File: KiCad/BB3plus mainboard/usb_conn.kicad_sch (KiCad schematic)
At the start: 55 parts, among them IC18 MIC2026A-1YM-TR, IC19 PTN5150AHXMP, IC20 TPS2068E, IC21 TPD2E001DRLR, IC22 TPD2E001DRLR, IC23 FUSB340TMX, Q7 2N7002, Q8 2N7002, X14 USB4056-03-A, X15 MGB0A1-1CDDB005H

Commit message: PE fault detection section updated
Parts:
- renumbered C111 to C112, C112 to C113, C113 to C114, C114 to C115, C115 to C116, C116 to C117, C117 to C118, C118 to C119, C119 to C120, C120 to C121, C121 to C122, C122 to C123, C123 to C124, C124 to C125, C125 to C126, C126 to C127, JP14 to JP16, JP15 to JP17, JP16 to JP18, JP17 to JP19
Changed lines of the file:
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@@
 		(in_pos_files yes)
 		(dnp no)
-		(property "Reference" "C116"
+		(property "Reference" "C117"
 			(at 94.234 84.074 0)
 			(show_name no)
@@
 			(project "BB3plus mainboard"
 				(path "/1df84e4f-233a-4f72-9418-c0020706bb76/c0a485a3-023d-4313-ae06-c16e1fdbf75a"
-					(reference "C116")
+					(reference "C117")
 					(unit 1)
 				)
@@
 		(in_pos_files yes)
 		(dnp no)
-		(property "Reference" "C115"
+		(property "Reference" "C116"
 			(at 85.725 142.875 0)
 			(show_name no)
@@
 			(project "BB3plus mainboard"
 				(path "/1df84e4f-233a-4f72-9418-c0020706bb76/c0a485a3-023d-4313-ae06-c16e1fdbf75a"
-					(reference "C115")
+					(reference "C116")
 					(unit 1)
 				)
@@
 		(in_pos_files yes)
 		(dnp no)
-		(property "Reference" "C117"
+		(property "Reference" "C118"
 			(at 109.474 68.834 0)
 			(show_name no)
@@
 			(project "BB3plus mainboard"
 				(path "/1df84e4f-233a-4f72-9418-c0020706bb76/c0a485a3-023d-4313-ae06-c16e1fdbf75a"
-					(reference "C117")
+					(reference "C118")
 					(unit 1)
 				)
@@
 		(in_pos_files yes)
 		(dnp no)
-		(property "Reference" "C125"
+		(property "Reference" "C126"
 			(at 228.6 60.325 90)
 			(show_name no)
@@
 			(project "BB3plus mainboard"
 				(path "/1df84e4f-233a-4f72-9418-c0020706bb76/c0a485a3-023d-4313-ae06-c16e1fdbf75a"
-					(reference "C125")
+					(reference "C126")
 					(unit 1)
 				)
@@
 		(in_pos_files yes)
 		(dnp no)
-		(property "Reference" "C122"
+		(property "Reference" "C123"
 			(at 228.6 42.545 90)
 			(show_name no)
@@
 			(project "BB3plus mainboard"
 				(path "/1df84e4f-233a-4f72-9418-c0020706bb76/c0a485a3-023d-4313-ae06-c16e1fdbf75a"
-					(reference "C122")
+					(reference "C123")
 					(unit 1)
 				)
@@
 		(in_pos_files yes)
 		(dnp no)
-		(property "Reference" "JP14"
+		(property "Reference" "JP16"
 			(at 59.69 67.31 0)
 			(show_name no)
@@
 			(project "BB3plus mainboard"
 				(path "/1df84e4f-233a-4f72-9418-c0020706bb76/c0a485a3-023d-4313-ae06-c16e1fdbf75a"
-					(reference "JP14")
+					(reference "JP16")
 					(unit 1)
 				)
@@
 		(in_pos_files yes)
 		(dnp no)
-		(property "Reference" "#SUPPLY065"
+		(property "Reference" "#SUPPLY068"
 			(at 177.8 73.66 0)
 			(hide yes)
@@
 			(project "BB3plus mainboard"
 				(path "/1df84e4f-233a-4f72-9418-c0020706bb76/c0a485a3-023d-4313-ae06-c16e1fdbf75a"
-					(reference "#SUPPLY065")
+					(reference "#SUPPLY068")
 					(unit 1)
 				)
@@
 		(in_pos_files yes)
 		(dnp no)
-		(property "Reference" "C111"
+		(property "Reference" "C112"
 			(at 28.575 34.29 0)
 			(show_name no)
@@
 			(project "BB3plus mainboard"
 				(path "/1df84e4f-233a-4f72-9418-c0020706bb76/c0a485a3-023d-4313-ae06-c16e1fdbf75a"
-					(reference "C111")
+					(reference "C112")
 					(unit 1)
 				)
@@
 		(in_pos_files yes)
 		(dnp no)
-		(property "Reference" "#SUPPLY067"
+		(property "Reference" "#SUPPLY070"
 			(at 205.74 73.66 0)
 			(hide yes)
@@
 			(project "BB3plus mainboard"
 				(path "/1df84e4f-233a-4f72-9418-c0020706bb76/c0a485a3-023d-4313-ae06-c16e1fdbf75a"
-					(reference "#SUPPLY067")
+					(reference "#SUPPLY070")
 					(unit 1)
 				)
@@
 		(in_pos_files yes)
 		(dnp no)
-		(property "Reference" "C112"
+		(property "Reference" "C113"
 			(at 35.56 31.75 0)
 			(show_name no)
@@
 			(project "BB3plus mainboard"
 				(path "/1df84e4f-233a-4f72-9418-c0020706bb76/c0a485a3-023d-4313-ae06-c16e1fdbf75a"
-					(reference "C112")
+					(reference "C113")
 					(unit 1)
 				)
@@
 		(in_pos_files yes)
 		(dnp no)
-		(property "Reference" "JP17"
+		(property "Reference" "JP19"
 			(at 59.69 90.17 0)
 			(show_name no)
@@
 			(project "BB3plus mainboard"
 				(path "/1df84e4f-233a-4f72-9418-c0020706bb76/c0a485a3-023d-4313-ae06-c16e1fdbf75a"
-					(reference "JP17")
+					(reference "JP19")
 					(unit 1)
 				)
@@
 		(in_pos_files yes)
 		(dnp no)
-		(property "Reference" "JP15"
+		(property "Reference" "JP17"
 			(at 59.69 72.39 0)
 			(show_name no)
@@
 			(project "BB3plus mainboard"
 				(path "/1df84e4f-233a-4f72-9418-c0020706bb76/c0a485a3-023d-4313-ae06-c16e1fdbf75a"
-					(reference "JP15")
+					(reference "JP17")
 					(unit 1)
 				)
@@
 		(in_pos_files yes)
 		(dnp no)
-		(property "Reference" "C121"
+		(property "Reference" "C122"
 			(at 155.194 45.974 0)
 			(show_name no)
@@
 			(project "BB3plus mainboard"
 				(path "/1df84e4f-233a-4f72-9418-c0020706bb76/c0a485a3-023d-4313-ae06-c16e1fdbf75a"
-					(reference "C121")
+					(reference "C122")
 					(unit 1)
 				)
@@
 		(in_pos_files yes)
 		(dnp no)
-		(property "Reference" "#SUPPLY064"
+		(property "Reference" "#SUPPLY067"
 			(at 177.8 43.18 0)
 			(hide yes)
@@
 			(project "BB3plus mainboard"
 				(path "/1df84e4f-233a-4f72-9418-c0020706bb76/c0a485a3-023d-4313-ae06-c16e1fdbf75a"
-					(reference "#SUPPLY064")
+					(reference "#SUPPLY067")
 					(unit 1)
 				)
@@
 		(in_pos_files yes)
 		(dnp no)
-		(property "Reference" "C119"
+		(property "Reference" "C120"
 			(at 116.84 45.72 0)
 			(show_name no)
@@
 			(project "BB3plus mainboard"
 				(path "/1df84e4f-233a-4f72-9418-c0020706bb76/c0a485a3-023d-4313-ae06-c16e1fdbf75a"
-					(reference "C119")
+					(reference "C120")
 					(unit 1)
 				)
@@
 		(in_pos_files yes)
 		(dnp no)
-		(property "Reference" "C113"
+		(property "Reference" "C114"
 			(at 48.26 167.005 0)
 			(show_name no)
@@
 			(project "BB3plus mainboard"
 				(path "/1df84e4f-233a-4f72-9418-c0020706bb76/c0a485a3-023d-4313-ae06-c16e1fdbf75a"
-					(reference "C113")
+					(reference "C114")
 					(unit 1)
 				)
@@
 		(in_pos_files yes)
 		(dnp no)
-		(property "Reference" "JP16"
+		(property "Reference" "JP18"
 			(at 59.69 77.47 0)
 			(show_name no)
@@
 			(project "BB3plus mainboard"
 				(path "/1df84e4f-233a-4f72-9418-c0020706bb76/c0a485a3-023d-4313-ae06-c16e1fdbf75a"
-					(reference "JP16")
+					(reference "JP18")
 					(unit 1)
 				)
@@
 		(in_pos_files yes)
 		(dnp no)
-		(property "Reference" "C126"
+		(property "Reference" "C127"
 			(at 271.78 37.465 90)
 			(show_name no)
@@
 			(project "BB3plus mainboard"
 				(path "/1df84e4f-233a-4f72-9418-c0020706bb76/c0a485a3-023d-4313-ae06-c16e1fdbf75a"
-					(reference "C126")
+					(reference "C127")
 					(unit 1)
 				)
@@
 		(in_pos_files yes)
 		(dnp no)
-		(property "Reference" "C118"
+		(property "Reference" "C119"
 			(at 109.474 84.074 0)
 			(show_name no)
@@
 			(project "BB3plus mainboard"
 				(path "/1df84e4f-233a-4f72-9418-c0020706bb76/c0a485a3-023d-4313-ae06-c16e1fdbf75a"
-					(reference "C118")
+					(reference "C119")
 					(unit 1)
 				)
@@
 		(in_pos_files yes)
 		(dnp no)
-		(property "Reference" "#SUPPLY066"
+		(property "Reference" "#SUPPLY069"
 			(at 205.74 43.18 0)
 			(hide yes)
@@
 			(project "BB3plus mainboard"
 				(path "/1df84e4f-233a-4f72-9418-c0020706bb76/c0a485a3-023d-4313-ae06-c16e1fdbf75a"
-					(reference "#SUPPLY066")
+					(reference "#SUPPLY069")
 					(unit 1)
 				)
@@
 		(in_pos_files yes)
 		(dnp no)
-		(property "Reference" "C123"
+		(property "Reference" "C124"
 			(at 228.6 45.085 90)
 			(show_name no)
@@
 			(project "BB3plus mainboard"
 				(path "/1df84e4f-233a-4f72-9418-c0020706bb76/c0a485a3-023d-4313-ae06-c16e1fdbf75a"
-					(reference "C123")
+					(reference "C124")
 					(unit 1)
 				)
@@
 		(in_pos_files yes)
 		(dnp no)
-		(property "Reference" "C120"
+		(property "Reference" "C121"
 			(at 127 95.885 90)
 			(show_name no)
@@
 			(project "BB3plus mainboard"
 				(path "/1df84e4f-233a-4f72-9418-c0020706bb76/c0a485a3-023d-4313-ae06-c16e1fdbf75a"
-					(reference "C120")
+					(reference "C121")
 					(unit 1)
 				)
@@
 		(in_pos_files yes)
 		(dnp no)
-		(property "Reference" "C124"
+		(property "Reference" "C125"
 			(at 228.6 57.785 90)
 			(show_name no)
@@
 			(project "BB3plus mainboard"
 				(path "/1df84e4f-233a-4f72-9418-c0020706bb76/c0a485a3-023d-4313-ae06-c16e1fdbf75a"
-					(reference "C124")
+					(reference "C125")
 					(unit 1)
 				)
@@
 		(in_pos_files yes)
 		(dnp no)
-		(property "Reference" "C114"
+		(property "Reference" "C115"
 			(at 85.725 130.175 0)
 			(show_name no)
@@
 			(project "BB3plus mainboard"
 				(path "/1df84e4f-233a-4f72-9418-c0020706bb76/c0a485a3-023d-4313-ae06-c16e1fdbf75a"
-					(reference "C114")
+					(reference "C115")
 					(unit 1)
 				)

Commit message: Various small changes
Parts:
- R78: now fitted; now in the parts list
- renumbered JP18 to JP16, JP16 to JP17, JP17 to JP18, X14 to X15, X15 to X16
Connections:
- net USBC_CONN_DET: no longer R78.2
- net at IC19.5 (ADR/CON_DET), JP16.1: now also R78.2
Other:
- moved on the sheet: JP16, TP13

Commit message: #24
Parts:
- D8: renamed from D14; now not fitted; now left out of the parts list
- renumbered C112 to C110, C113 to C111, C114 to C112, C115 to C113, C116 to C114, C117 to C115, C118 to C116, C119 to C117, C120 to C118, C121 to C119, C122 to C120, C123 to C121, C124 to C122, C125 to C123, C126 to C124, C127 to C125, IC18 to IC15, IC19 to IC16, IC20 to IC17, IC21 to IC18, IC22 to IC19, IC23 to IC20, JP16 to JP15, JP17 to JP16, JP18 to JP17, JP19 to JP18, R78 to R75, R79 to R76, R80 to R77, R81 to R78, R82 to R79, R83 to R80, R84 to R81, R85 to R82, R86 to R83, R87 to R84, R88 to R85, R89 to R86, R90 to R87

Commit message: USB CC wiring updated
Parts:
- removed JP18: 10129378-902001BLF, PCM_EEZ_SMD:JP2 open (0603), symbol PCM_EEZ_unsorted:JP2 open
- added JP15: (no value), PCM_EEZ_SMD:JP3 shorted (0603), symbol PCM_EEZ_unsorted:JP3 shorted
- added R78: 10K, PCM_EEZ_passives:R_0603_1608Metric, symbol PCM_EEZ_passives:R-EU
- C110, C113, C114: LCSC - -> C336508
- JP16: renamed from JP15; value 10129378-902001BLF -> (none); DigiKey 10129378-902001BLF-ND -> (none); LCSC C3324910 -> (none); Label I2C HUB -> (none); Mouser 649-1012937890201BLF -> (none); TME ZL201-02G -> (none)
- JP17: renamed from JP16; value 10129378-902001BLF -> (none); footprint PCM_EEZ_SMD:JP2 open (0603) -> PCM_EEZ_SMD:JP2 shorted (0603); symbol PCM_EEZ_unsorted:JP2 open -> PCM_EEZ_unsorted:JP2 shorted; DigiKey 10129378-902001BLF-ND -> (none); LCSC C3324910 -> (none); Mouser 649-1012937890201BLF -> (none); TME ZL201-02G -> (none)
- JP18: renamed from JP17; value 10129378-902001BLF -> (none); footprint PCM_EEZ_SMD:JP2 open (0603) -> PCM_EEZ_SMD:JP2 shorted (0603); symbol PCM_EEZ_unsorted:JP2 open -> PCM_EEZ_unsorted:JP2 shorted; DigiKey 10129378-902001BLF-ND -> (none); LCSC C3324910 -> (none); Label I2C HUB -> (none); Mouser 649-1012937890201BLF -> (none); TME ZL201-02G -> (none)
- LED7: now fitted
- R85: renamed from R84; value 1K -> 1K8; DigiKey 13-RC0603FR-131KLCT-ND -> 13-RC0603FR-131K8LCT-ND; LCSC C21190 -> C4177; Mouser 603-RC0603FR-131KL -> 603-RC0603FR-131K8L; TME CQ0603-1K-1% -> SMD0603-1K8-1%; now fitted; now in the parts list
- X15: Label USB-C DRD -> USB-C
- renumbered R78 to R79, R79 to R80, R80 to R81, R81 to R82, R82 to R83, R83 to R84, R85 to R86, R86 to R87, R87 to R88
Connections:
- net +3V3: now also JP15.NO, R78.1; no longer R75.1
- net GND: now also JP15.NC
- net at IC16.3 (PORT): now also R78.2
- new net: JP15.COM, R75.1
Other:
- moved on the sheet: JP16, R75

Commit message: #25
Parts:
- X15: value USB4056-03-A -> USB4080-03-A; footprint PCM_EEZ_connectors:USB4056-03-A_REVA2 -> PCM_EEZ_connectors:USB4080-03-A_REVA1; DigiKey 2073-USB4056-03-ACT-ND -> 2073-USB4080-03-ACT-ND; LCSC C7407280 -> C48533151; Mouser 640-USB4056-03-A -> 640-USB4080-03-A; TME USB4056-03-A -> USB4080-03-A
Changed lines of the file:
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@@
 			)
 		)
-		(property "Value" "USB4056-03-A"
+		(property "Value" "USB4080-03-A"
 			(at 137.795 92.075 0)
 			(show_name no)
@@
 			)
 		)
-		(property "Footprint" "PCM_EEZ_connectors:USB4056-03-A_REVA2"
+		(property "Footprint" "PCM_EEZ_connectors:USB4080-03-A_REVA1"
 			(at 147.32 99.06 0)
 			(hide yes)
@@
 			)
 		)
-		(property "Description" "USB-C USB 3.2 Rec, Horz, Hybrid PCB Top Mount, T+R"
+		(property "Description" ""
 			(at 147.32 96.52 0)
 			(hide yes)
@@
 			)
 		)
-		(property "DigiKey" "2073-USB4056-03-ACT-ND"
+		(property "DigiKey" "2073-USB4080-03-ACT-ND"
 			(at 147.32 101.6 0)
 			(hide yes)
@@
 			)
 		)
-		(property "Mouser" "640-USB4056-03-A"
+		(property "Mouser" "640-USB4080-03-A"
 			(at 147.32 104.14 0)
 			(hide yes)
@@
 			)
 		)
-		(property "TME" "USB4056-03-A"
+		(property "TME" "USB4080-03-A"
 			(at 147.32 106.68 0)
 			(hide yes)
@@
 			)
 		)
-		(property "LCSC" "C7407280"
+		(property "LCSC" "C48533151"
 			(at 147.32 109.22 0)
 			(hide yes)

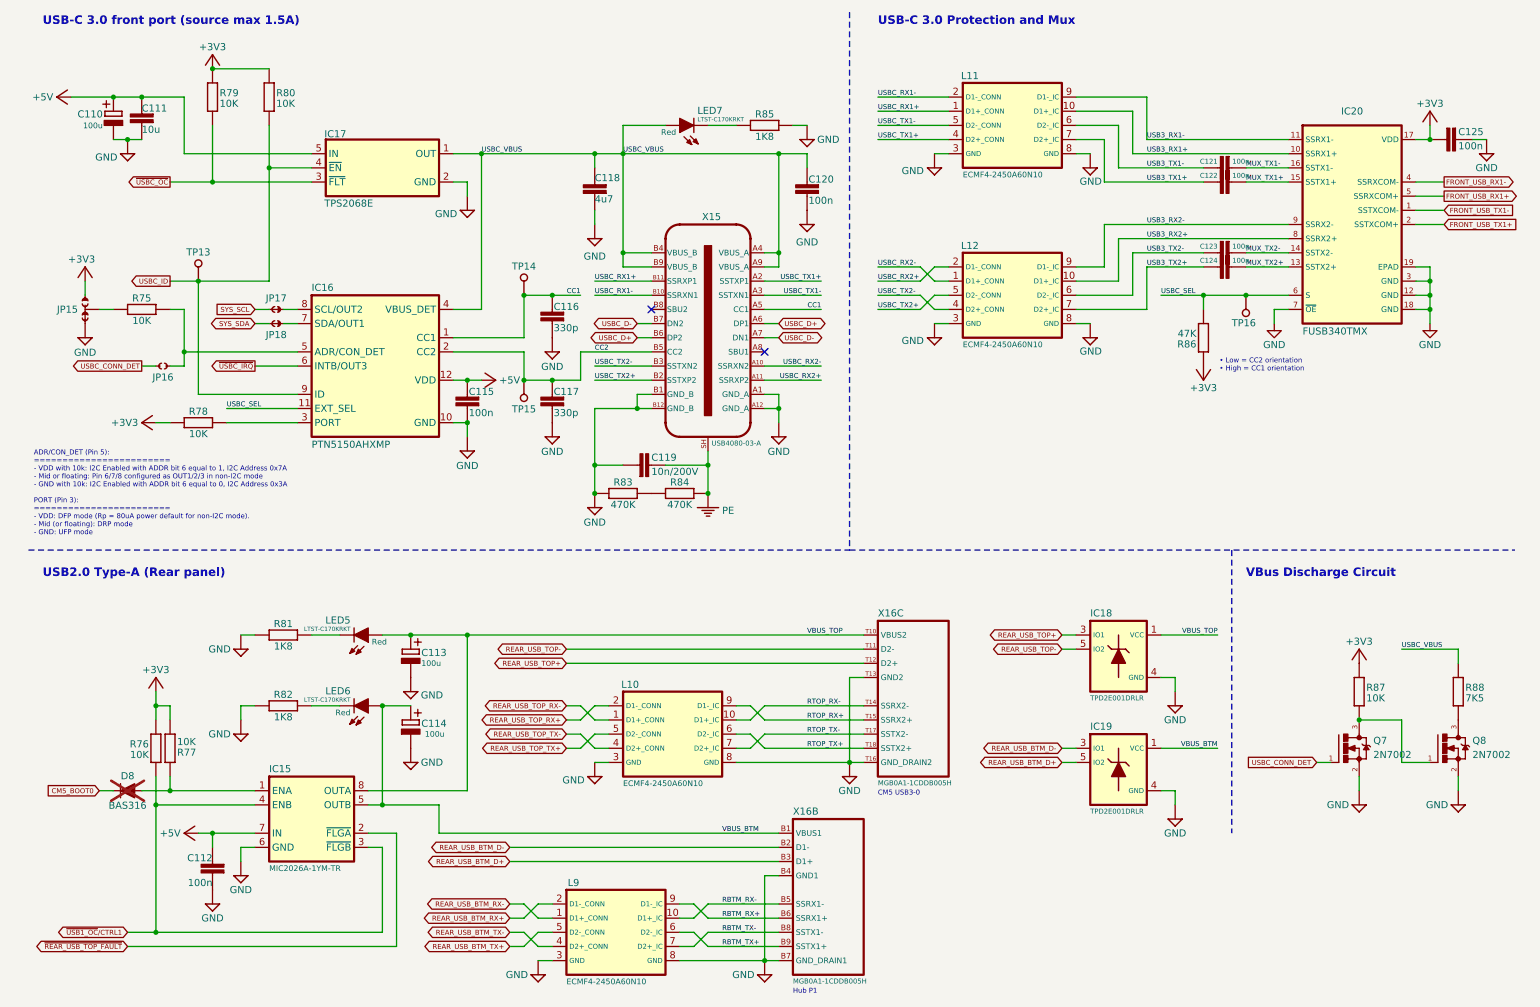
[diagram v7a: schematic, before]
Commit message: Rear USB & Ethernet updated
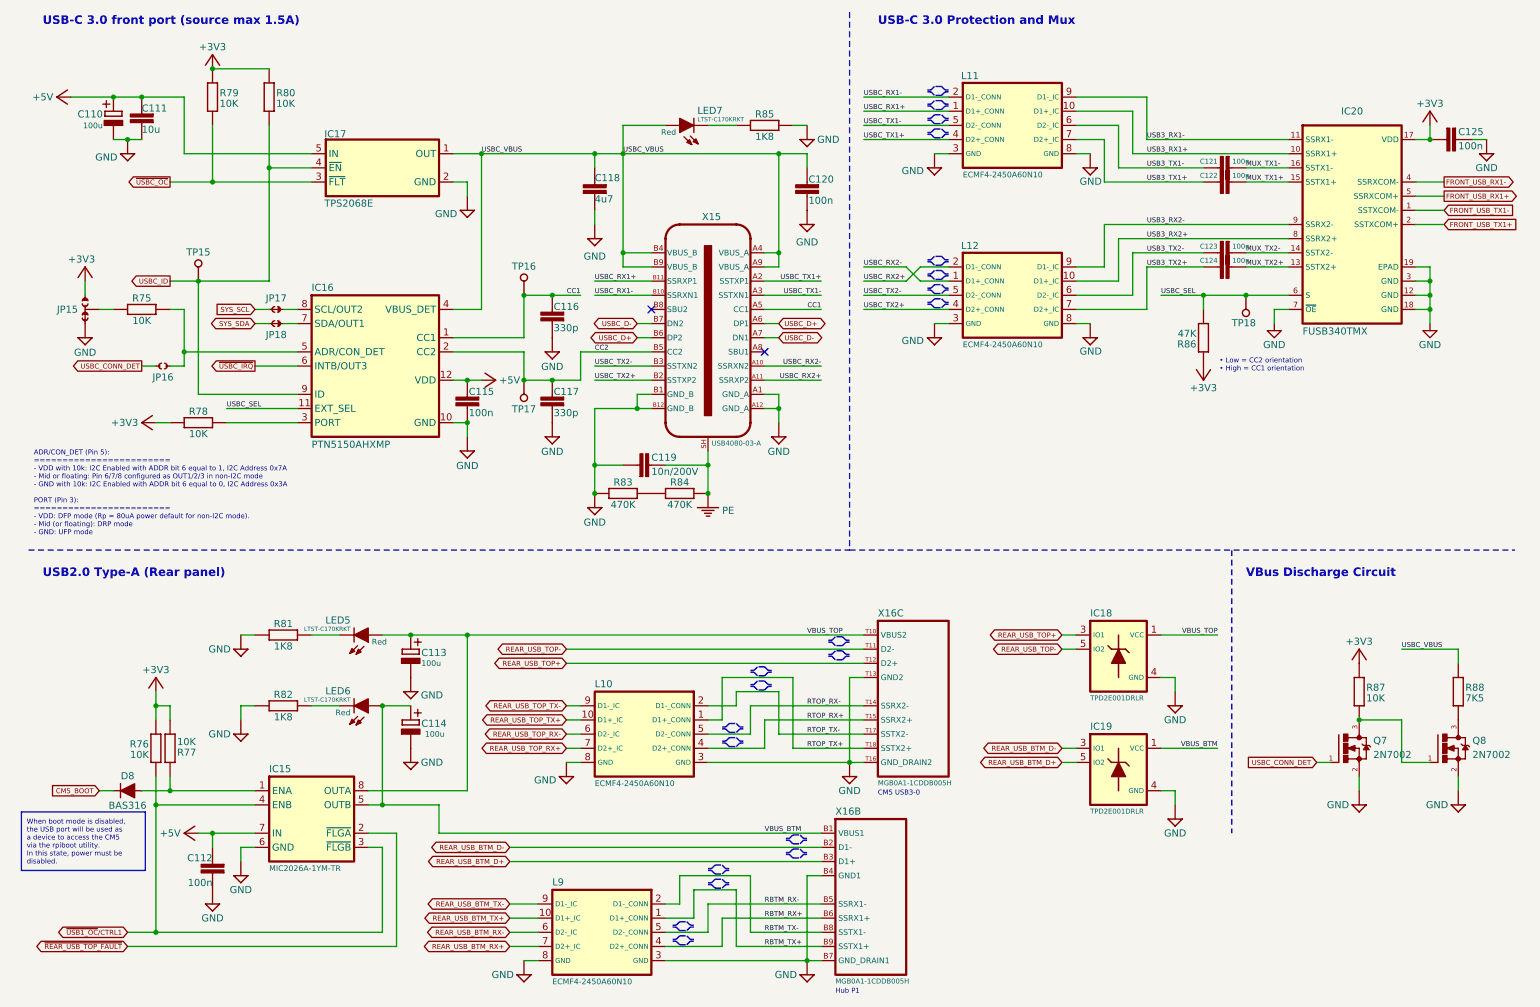
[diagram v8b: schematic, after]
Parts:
- D8: now fitted; now in the parts list
- renumbered TP13 to TP15, TP14 to TP16, TP15 to TP17, TP16 to TP18
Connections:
- net RBTM_RX+: now also L9.4 (D2+_CONN); no longer L9.9 (D1-_IC)
- net RBTM_RX-: now also L9.5 (D2-_CONN); no longer L9.10 (D1+_IC)
- net RBTM_TX+: now also L9.1 (D1+_CONN); no longer L9.6 (D2-_IC)
- net RBTM_TX-: now also L9.2 (D1-_CONN); no longer L9.7 (D2+_IC)
- net REAR_USB_BTM_RX+: now also L9.7 (D2+_IC); no longer L9.2 (D1-_CONN)
- net REAR_USB_BTM_RX-: now also L9.6 (D2-_IC); no longer L9.1 (D1+_CONN)
- net REAR_USB_BTM_TX+: now also L9.10 (D1+_IC); no longer L9.5 (D2-_CONN)
- net REAR_USB_BTM_TX-: now also L9.9 (D1-_IC); no longer L9.4 (D2+_CONN)
- net REAR_USB_TOP_RX+: now also L10.7 (D2+_IC); no longer L10.2 (D1-_CONN)
- net REAR_USB_TOP_RX-: now also L10.6 (D2-_IC); no longer L10.1 (D1+_CONN)
- net REAR_USB_TOP_TX+: now also L10.10 (D1+_IC); no longer L10.5 (D2-_CONN)
- net REAR_USB_TOP_TX-: now also L10.9 (D1-_IC); no longer L10.4 (D2+_CONN)
- net RTOP_RX+: now also L10.4 (D2+_CONN); no longer L10.9 (D1-_IC)
- net RTOP_RX-: now also L10.5 (D2-_CONN); no longer L10.10 (D1+_IC)
- net RTOP_TX+: now also L10.1 (D1+_CONN); no longer L10.6 (D2-_IC)
- net RTOP_TX-: now also L10.2 (D1-_CONN); no longer L10.7 (D2+_IC)
- net USBC_TX2+: now also L12.4 (D2+_CONN); no longer L12.5 (D2-_CONN)
- net USBC_TX2-: now also L12.5 (D2-_CONN); no longer L12.4 (D2+_CONN)
- net CM5_BOOT0 renamed CM5_BOOT
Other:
- moved on the sheet: L10, L9, X16B
